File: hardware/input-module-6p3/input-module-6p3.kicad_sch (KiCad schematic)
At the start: 0 parts

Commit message: Add input module schematic and 10-pin input header
- input-module-6p3 schematic: two Neutrik NMJ6HCD2 switched jacks
  (L/MONO, R) with R-to-L mono normalling, and a 1x10 Molex KK 254
  header to the channel card. ERC clean.
- Decision 67: cutoff CV jack moves to the channel card's filter
  section, on the top panel next to CUTOFF.
- Decision 68: input header grows to 10 pins; pins 8-9 reserved for
  the stereo pre-fader direct output (backlog), pin 10 AGND.
- parts.csv: SX-CONN-001 jack and SX-CONN-002 header.
- .gitignore: kicad-mcp-pro working files, reports and backups.

Co-Authored-By: Claude Opus 5.5 <noreply@anthropic.com>
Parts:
- added J1: L/MONO IN, Connector_Audio:Jack_6.35mm_Neutrik_NMJ6HCD2_Horizontal, symbol Connector_Audio:AudioJack3_Switch
- added J2: R IN, Connector_Audio:Jack_6.35mm_Neutrik_NMJ6HCD2_Horizontal, symbol Connector_Audio:AudioJack3_Switch
- added J3: TO CHANNEL CARD, Connector_Molex:Molex_KK-254_AE-6410-10A_1x10_P2.54mm_Vertical, symbol Connector_Generic:Conn_01x10
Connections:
- new net AGND: J1.S, J2.S, J3.1 (Pin_1), J3.10 (Pin_10), J3.4 (Pin_4), J3.7 (Pin_7)
- new net L+: J1.T, J2.TN, J3.2 (Pin_2)
- new net L-: J1.R, J2.RN, J3.3 (Pin_3)
- new net R+: J2.T, J3.5 (Pin_5)
- new net R-: J2.R, J3.6 (Pin_6)
- no-connect marks 0 -> 6
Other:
- company: (none) -> Syntsamix
- title: (none) -> Input module, 6.3 mm

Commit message: System: cost review and cost control (decisions 132-137)
Rean NYS216 jacks with a new footprint (132), through-hole parts hand-soldered (133), E24 values owned per board (134), live-device cost principle (135), /cost with the cost-controller sub-agent, tools/costs.py and a private ledger of realized costs (136), JLCPCB fee-free parts first (137).

Co-Authored-By: Claude Opus 5.5 <noreply@anthropic.com>
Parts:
- J1, J2: footprint Connector_Audio:Jack_6.35mm_Neutrik_NMJ6HCD2_Horizontal -> syntsamix:Jack_6.35mm_Rean_NYS216_Horizontal; MPN NMJ6HCD2 -> NYS216; Manufacturer Neutrik -> Rean; ProjectPN SX-CONN-001 -> SX-CONN-015
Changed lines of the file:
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@@
 			)
 		)
-		(property "Footprint" "Connector_Audio:Jack_6.35mm_Neutrik_NMJ6HCD2_Horizontal"
+		(property "Footprint" "syntsamix:Jack_6.35mm_Rean_NYS216_Horizontal"
 			(at 50.8 96.52 0)
 			(hide yes)
@@
 			)
 		)
-		(property "ProjectPN" "SX-CONN-001"
+		(property "ProjectPN" "SX-CONN-015"
 			(at 50.8 96.52 0)
 			(hide yes)
@@
 			)
 		)
-		(property "Manufacturer" "Neutrik"
+		(property "Manufacturer" "Rean"
 			(at 50.8 96.52 0)
 			(hide yes)
@@
 			)
 		)
-		(property "MPN" "NMJ6HCD2"
+		(property "MPN" "NYS216"
 			(at 50.8 96.52 0)
 			(hide yes)
@@
 			)
 		)
-		(property "Footprint" "Connector_Audio:Jack_6.35mm_Neutrik_NMJ6HCD2_Horizontal"
+		(property "Footprint" "syntsamix:Jack_6.35mm_Rean_NYS216_Horizontal"
 			(at 50.8 60.96 0)
 			(hide yes)
@@
 			)
 		)
-		(property "ProjectPN" "SX-CONN-001"
+		(property "ProjectPN" "SX-CONN-015"
 			(at 50.8 60.96 0)
 			(hide yes)
@@
 			)
 		)
-		(property "Manufacturer" "Neutrik"
+		(property "Manufacturer" "Rean"
 			(at 50.8 60.96 0)
 			(hide yes)
@@
 			)
 		)
-		(property "MPN" "NMJ6HCD2"
+		(property "MPN" "NYS216"
 			(at 50.8 60.96 0)
 			(hide yes)

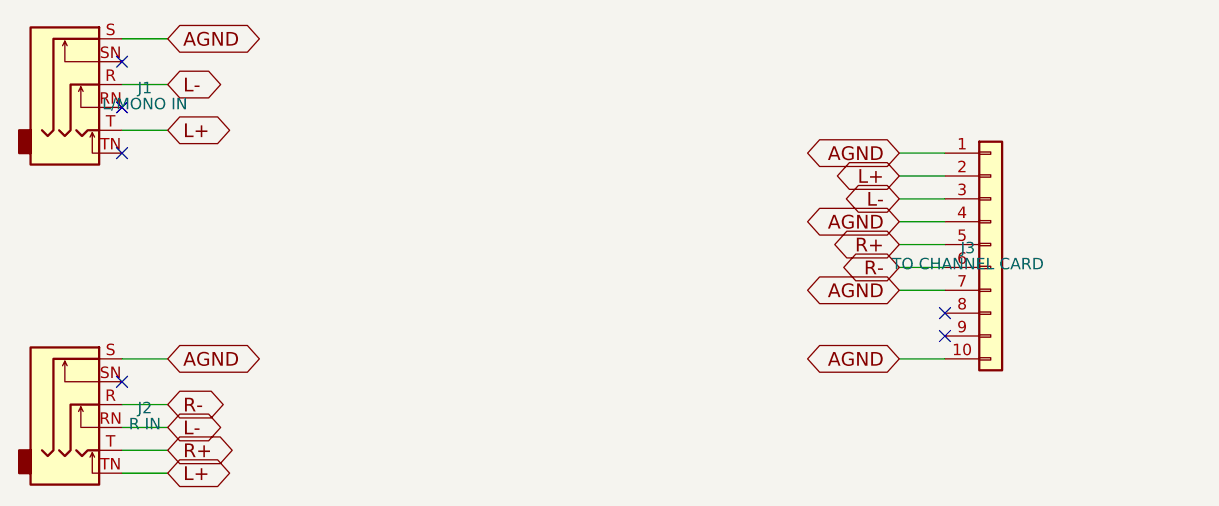
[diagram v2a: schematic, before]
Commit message: Input module: input header J3 redrawn as the Adam Tech 2x6 box header on the stock KiCad parts (decision 181)
Co-Authored-By: Claude Opus 5.5 <noreply@anthropic.com>
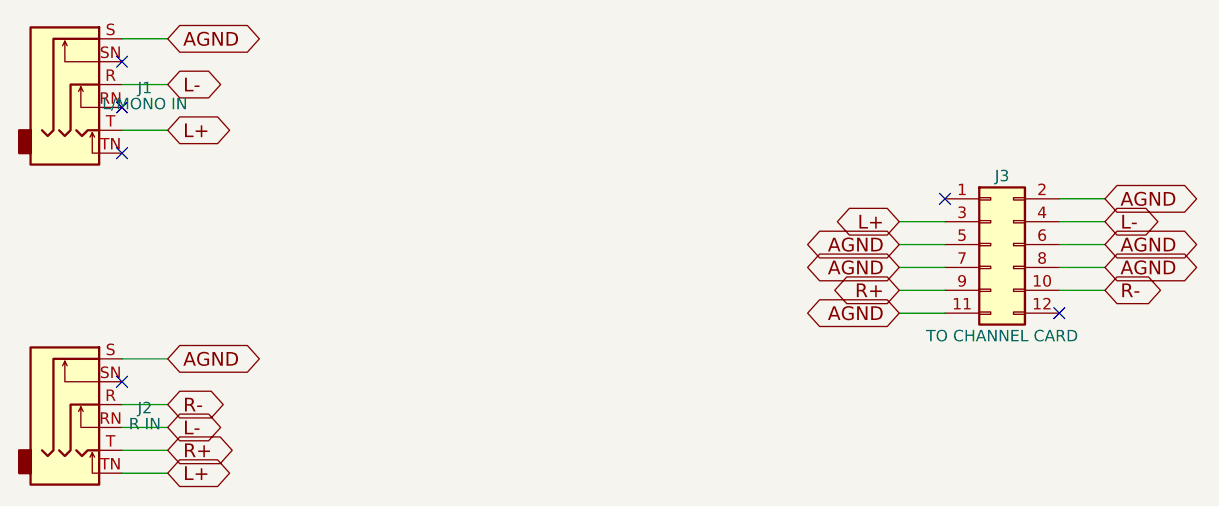
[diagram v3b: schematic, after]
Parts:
- removed J3: TO CHANNEL CARD, Connector_Molex:Molex_KK-254_AE-6410-10A_1x10_P2.54mm_Vertical, symbol Connector_Generic:Conn_01x10
- added J3: TO CHANNEL CARD, Connector_IDC:IDC-Header_2x06_P2.54mm_Vertical, symbol Connector_Generic:Conn_02x06_Odd_Even
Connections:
- net AGND: now also J3.11 (Pin_11), J3.2 (Pin_2), J3.5 (Pin_5), J3.6 (Pin_6), J3.7 (Pin_7), J3.8 (Pin_8)
- net L+: now also J3.3 (Pin_3)
- net L-: now also J3.4 (Pin_4)
- net R+: now also J3.9 (Pin_9)
- net R-: now also J3.10 (Pin_10)
